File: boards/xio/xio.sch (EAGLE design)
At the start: 152 parts, among them Y2 NX3225SA-12.000MHZ-STD-CSR-1

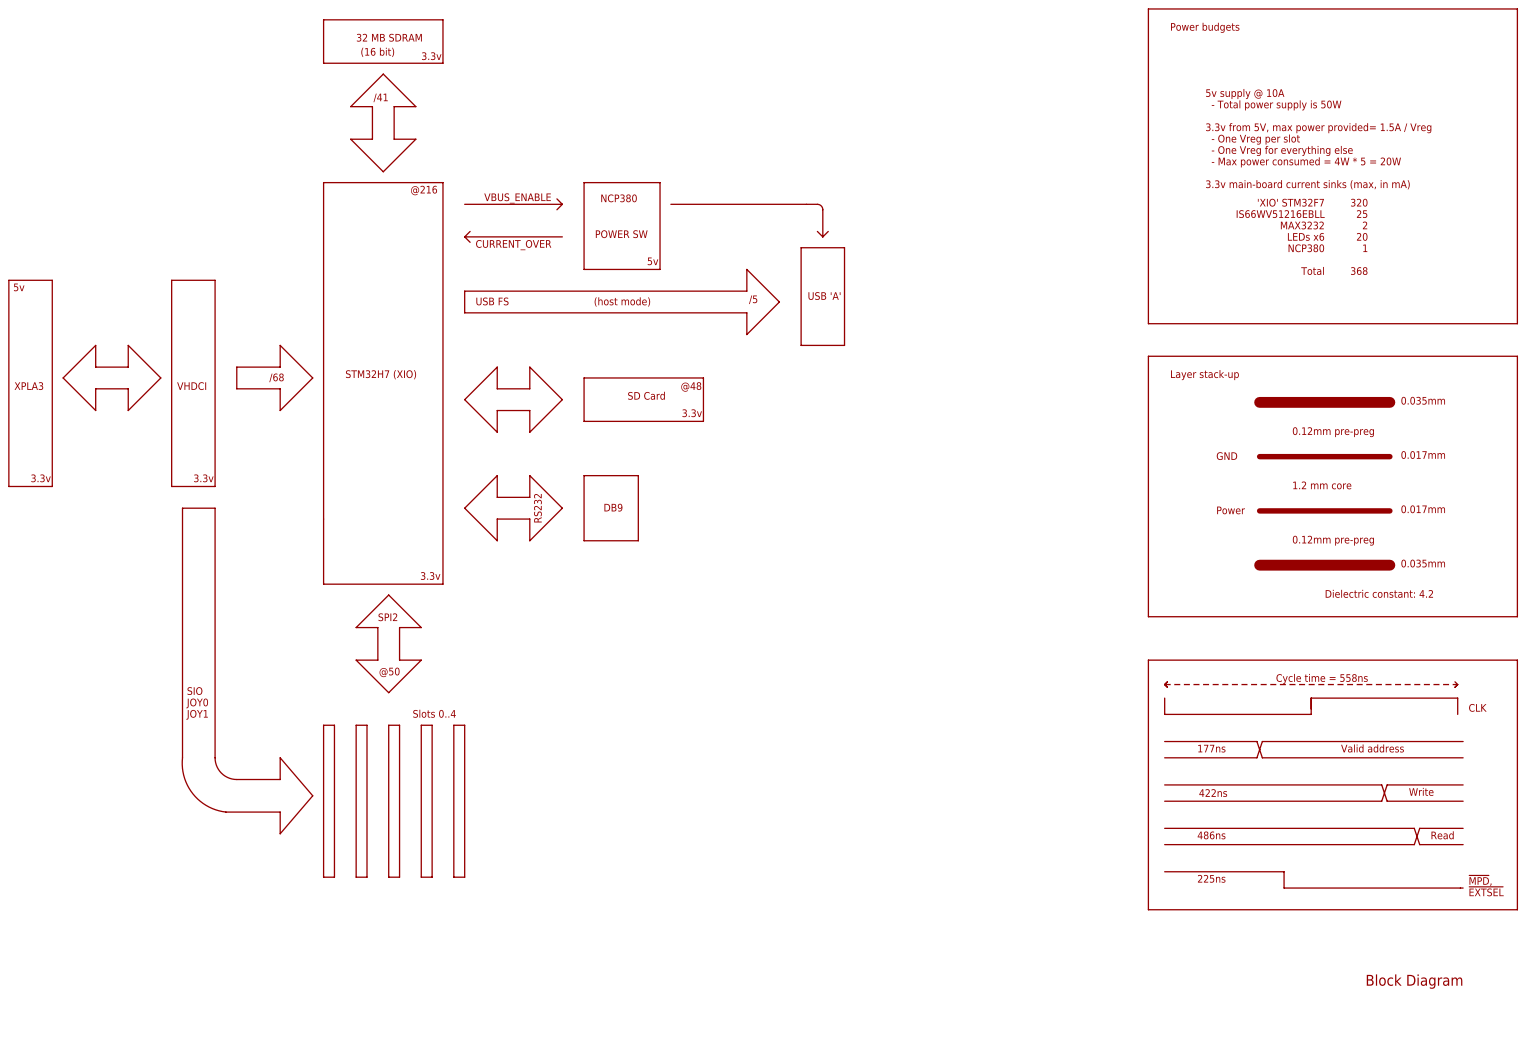
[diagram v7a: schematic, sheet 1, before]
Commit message: Update to Eagle 1.1 Update the block diagram
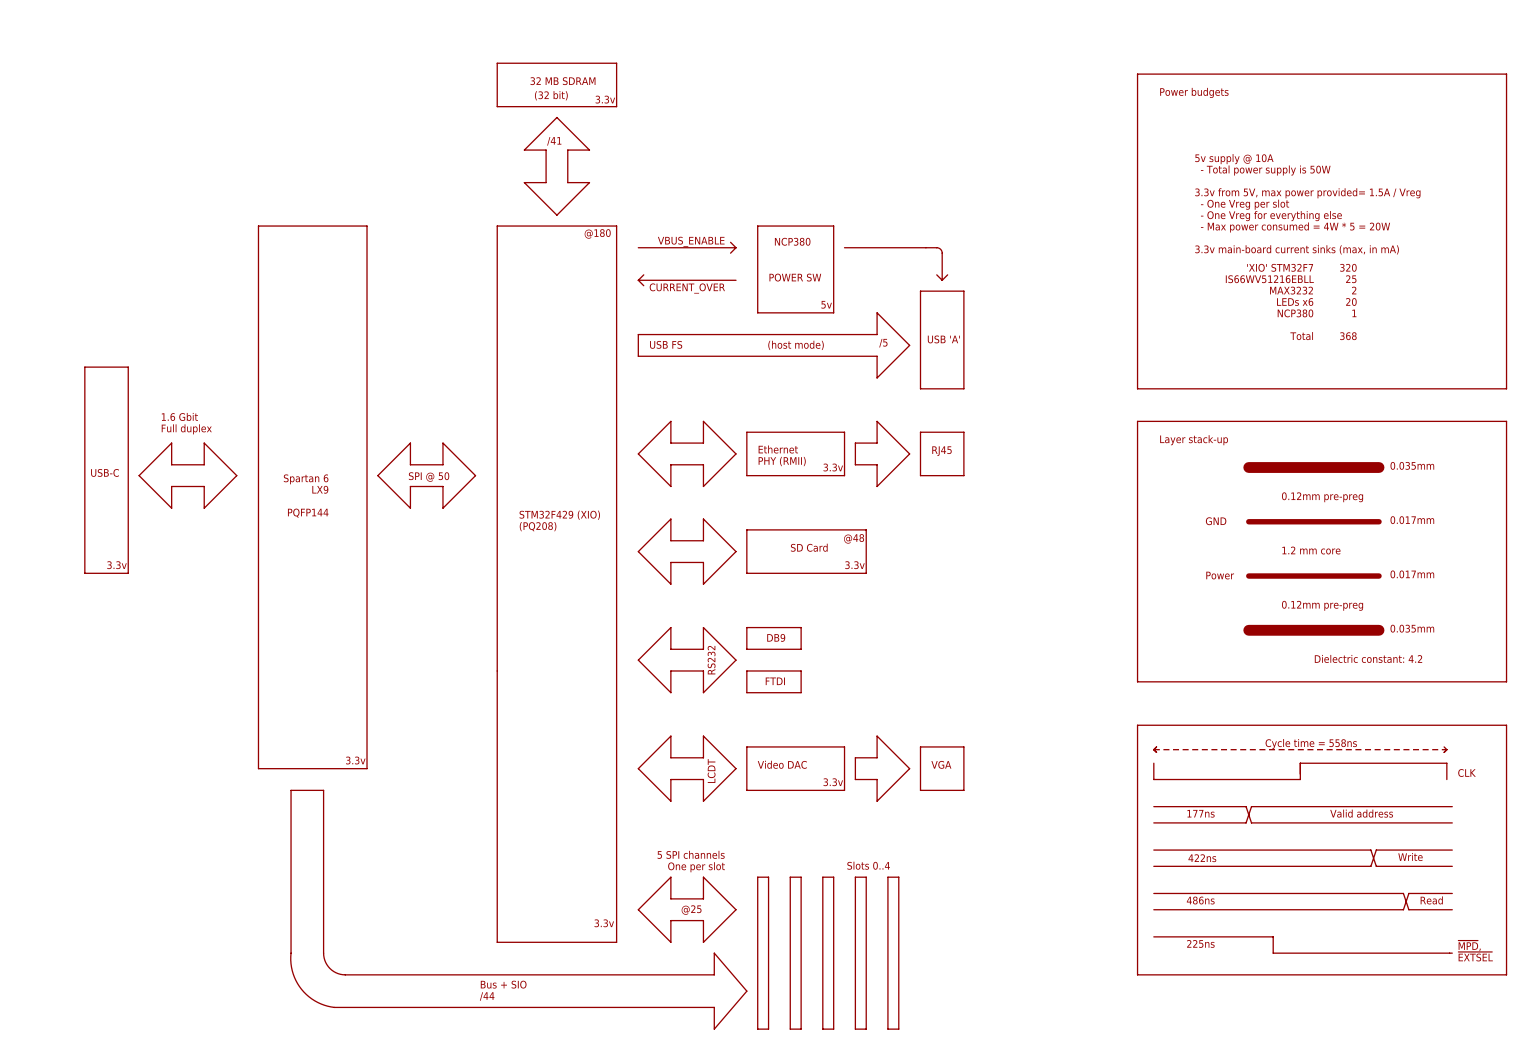
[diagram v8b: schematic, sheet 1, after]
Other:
- note added: "(32 bit)"
- note added: "0.035 mm 0.12 mm 10 mil 7 mil 4.4 90.5 ohms"
- note added: "1.6 Gbit Full duplex"
- note added: "5 SPI channels One per slot"
- note added: "@180"
- note added: "@25"
- note added: "Bus + SIO /44"
- note added: "Ethernet PHY (RMII)"
- note added: "FTDI"
- note added: "LCDT"
- note added: "RJ45"
- note added: "SPI @ 50"
- note added: "STM32F429 (XIO) (PQ208)"
- note added: "Spartan 6 LX9 PQFP144"
- note added: "USB-C"
- note added: "VGA"
- note added: "Video DAC"
- note removed: "(16 bit)"
- note removed: "/68"
- note removed: "0.035 mm 0.12 mm 10 mil 8 mil 4.4 91.7 ohms"
- note removed: "@216"
- note removed: "@50"
- note removed: "Block Diagram"
- note removed: "SIO JOY0 JOY1"
- note removed: "SPI2"
- note removed: "STM32H7 (XIO)"
- note removed: "VHDCI"
- note removed: "XPLA3"
